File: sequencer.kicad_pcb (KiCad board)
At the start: 2 copper layers, 24 parts, among them SW1 B3S-1000P, SW2 B3S-1000P, SW3 B3S-1000P, SW4 B3S-1000P, SW5 B3S-1000P, SW6 B3S-1000P, SW7 B3S-1000P, SW8 B3S-1000P, SW9 B3S-1000P, U3 STM32F031K6Tx, U6 L78L05_SOT89, U7 L78L33_SOT89, Y1 8MHz

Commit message: mostly complete placement
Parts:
- removed the U6 at (78.5, 55.5)
- removed Y1: 8MHz, Crystal:Crystal_SMD_HC49-SD
- added C1: 100n, Capacitor_SMD:C_0603_1608Metric, B.Cu at (86.9, 93.0)
- added C10: 100n, Capacitor_SMD:C_0603_1608Metric, B.Cu at (103.0, 83.0)
- added C11: 100n, Capacitor_SMD:C_0603_1608Metric, B.Cu at (118.0, 83.0)
- added C13: 100n, Capacitor_SMD:C_0603_1608Metric, B.Cu at (147.0, 83.0)
- added C14: 100n, Capacitor_SMD:C_0603_1608Metric, B.Cu at (162.0, 83.0)
- added C15: 100n, Capacitor_SMD:C_0603_1608Metric, B.Cu at (177.0, 83.0)
- added C16: 100n, Capacitor_SMD:C_0603_1608Metric, B.Cu at (192.0, 83.0)
- added C17: 100n, Capacitor_SMD:C_0603_1608Metric, B.Cu at (154.0, 145.0)
- added C18: 100n, Capacitor_SMD:C_0603_1608Metric, B.Cu at (163.0, 143.0)
- added C19: 100n, Capacitor_SMD:C_0603_1608Metric, B.Cu at (202.0, 108.0)
- added C2: 100n, Capacitor_SMD:C_0603_1608Metric, B.Cu at (101.7, 93.0)
- added C20: 10n, Capacitor_SMD:C_0603_1608Metric, B.Cu at (149.0, 70.0)
- added C26: 100n, Capacitor_SMD:C_0603_1608Metric, B.Cu at (107.9, 119.0)
- added C27: 100n, Capacitor_SMD:C_0603_1608Metric, B.Cu at (122.8, 119.0)
- added C28: 330n, Capacitor_SMD:C_0805_2012Metric, B.Cu at (121.0, 39.0)
- added C29: 100n, Capacitor_SMD:C_0603_1608Metric, B.Cu at (121.0, 46.0)
- added C3: 100n, Capacitor_SMD:C_0603_1608Metric, B.Cu at (116.5, 93.0)
- added C30: 330n, Capacitor_SMD:C_0805_2012Metric, B.Cu at (117.0, 61.0)
- added C31: 100n, Capacitor_SMD:C_0603_1608Metric, B.Cu at (124.0, 61.0)
- added C4: 100n, Capacitor_SMD:C_0603_1608Metric, B.Cu at (131.3, 93.0)
- added C5: 100n, Capacitor_SMD:C_0603_1608Metric, B.Cu at (146.2, 93.0)
- added C8: 100n, Capacitor_SMD:C_0603_1608Metric, B.Cu at (190.6, 93.0)
- added C9: 100n, Capacitor_SMD:C_0603_1608Metric, B.Cu at (88.0, 83.0)
- added D3: Inolux_IN-PI554FCH, LED_SMD:LED_Inolux_IN-PI554FCH_PLCC4_5.0x5.0mm_P3.2mm, F.Cu at (117.8, 78.5)
- added D4: Inolux_IN-PI554FCH, LED_SMD:LED_Inolux_IN-PI554FCH_PLCC4_5.0x5.0mm_P3.2mm, F.Cu at (132.6, 78.5)
- added D5: Inolux_IN-PI554FCH, LED_SMD:LED_Inolux_IN-PI554FCH_PLCC4_5.0x5.0mm_P3.2mm, F.Cu at (147.4, 78.5)
- added D6: Inolux_IN-PI554FCH, LED_SMD:LED_Inolux_IN-PI554FCH_PLCC4_5.0x5.0mm_P3.2mm, F.Cu at (162.2, 78.5)
- added D7: Inolux_IN-PI554FCH, LED_SMD:LED_Inolux_IN-PI554FCH_PLCC4_5.0x5.0mm_P3.2mm, F.Cu at (177.0, 78.5)
- added D8: Inolux_IN-PI554FCH, LED_SMD:LED_Inolux_IN-PI554FCH_PLCC4_5.0x5.0mm_P3.2mm, F.Cu at (191.8, 78.5)
- added D9: red, LED_SMD:LED_0603_1608Metric, B.Cu at (99.0, 48.5)
- added G***: LOGO, Symbol_CreativeCommons:CC-BY-SA_SolderMaskTop_Small, B.Cu at (185.0, 68.0)
- added J1: AudioJack2_SwitchT, Connector_Audio:Jack_3.5mm_QingPu_WQP-PJ398SM_Vertical_CircularHoles, F.Cu at (96.0, 110.2)
- added J2: AudioJack2_SwitchT, Connector_Audio:Jack_3.5mm_QingPu_WQP-PJ398SM_Vertical_CircularHoles, F.Cu at (184.0, 110.2)
- added J3: AudioJack2_SwitchT, Connector_Audio:Jack_3.5mm_QingPu_WQP-PJ398SM_Vertical_CircularHoles, F.Cu at (172.9, 110.2)
- added J4: Conn_ARM_JTAG_SWD_10, Connector_PinHeader_1.27mm:PinHeader_2x05_P1.27mm_Vertical_SMD, B.Cu at (119.0, 70.0)
- added J5: Conn_01x06_Male, Connector_PinHeader_2.54mm:PinHeader_1x06_P2.54mm_Vertical, F.Cu at (139.3, 67.0)
- added J6: Conn_01x02_Male, Connector_Molex:Molex_SL_171971-0002_1x02_P2.54mm_Vertical, B.Cu at (93.0, 70.0)
- added R1: 10k, Resistor_SMD:R_0603_1608Metric, B.Cu at (104.0, 48.5)
- added R3: 1k, Resistor_SMD:R_0603_1608Metric, B.Cu at (101.0, 123.0)
- added REF**: MountingHole_3.2mm_M3, MountingHole:MountingHole_3.2mm_M3, F.Cu at (85.0, 70.0)
- added REF**: MountingHole_3.2mm_M3, MountingHole:MountingHole_3.2mm_M3, F.Cu at (195.0, 70.0)
- added REF**: MountingHole_3.2mm_M3, MountingHole:MountingHole_3.2mm_M3, F.Cu at (85.0, 120.0)
- added REF**: MountingHole_3.2mm_M3, MountingHole:MountingHole_3.2mm_M3, F.Cu at (195.0, 120.0)
- added RV1: 10k, Potentiometer_THT:Potentiometer_Bourns_PTV09A-1_Single_Vertical, F.Cu at (90.7, 96.0)
- added RV10: 10k, Potentiometer_THT:Potentiometer_Bourns_PTV09A-1_Single_Vertical, F.Cu at (126.5, 122.0)
- added RV2: 10k, Potentiometer_THT:Potentiometer_Bourns_PTV09A-1_Single_Vertical, F.Cu at (105.5, 96.0)
- added RV3: 10k, Potentiometer_THT:Potentiometer_Bourns_PTV09A-1_Single_Vertical, F.Cu at (120.3, 96.0)
- added RV4: 10k, Potentiometer_THT:Potentiometer_Bourns_PTV09A-1_Single_Vertical, F.Cu at (135.1, 96.0)
- added RV5: 10k, Potentiometer_THT:Potentiometer_Bourns_PTV09A-1_Single_Vertical, F.Cu at (149.9, 96.0)
- added RV6: 10k, Potentiometer_THT:Potentiometer_Bourns_PTV09A-1_Single_Vertical, F.Cu at (164.7, 96.0)
- added RV7: 10k, Potentiometer_THT:Potentiometer_Bourns_PTV09A-1_Single_Vertical, F.Cu at (179.5, 96.0)
- added RV8: 10k, Potentiometer_THT:Potentiometer_Bourns_PTV09A-1_Single_Vertical, F.Cu at (194.3, 96.0)
- added RV9: 10k, Potentiometer_THT:Potentiometer_Bourns_PTV09A-1_Single_Vertical, F.Cu at (111.7, 122.0)
- added SW10: SW_SPST, Button_Switch_THT_gkeeth:SW_Toggle_SPST_NKK_M2011xxx03, F.Cu at (92.0, 58.0)
- added U1: LM358, Package_SO:SOIC-8_3.9x4.9mm_P1.27mm, B.Cu at (194.0, 110.0)
- added U2: 74HC4051, Package_SO:SOIC-16_3.9x9.9mm_P1.27mm, B.Cu at (154.0, 136.0)
- added U4: 74HCT14, Package_SO:SOIC-14_3.9x8.7mm_P1.27mm, B.Cu at (163.0, 136.0)
- added U5: L78L05_SOT89, Package_TO_SOT_SMD:SOT-89-3, B.Cu at (121.7, 42.5)
- added X1: ASV-8.000MHz, Oscillator:Oscillator_SMD_Abracon_ASV-4Pin_7.0x5.1mm, B.Cu at (144.0, 71.0)
- C12, U3: moved to B.Cu
- C21: renamed from C5; moved to B.Cu
- C22: renamed from C8; moved to B.Cu
- C23: renamed from C9; moved to B.Cu
- C24: renamed from C10; moved to B.Cu
- C25: renamed from C11; moved to B.Cu
- C6, C7: value 27p -> 100n; moved to B.Cu
- R2: renamed from R10; moved to B.Cu
- SW1, SW2, SW3, SW4, SW5, SW6, SW7, SW8, SW9: value B3S-1000P -> OS102011MS2QN1; footprint Button_Switch_SMD:SW_SPST_B3S-1000 -> Button_Switch_THT:SW_Slide_1P2T_CK_OS102011MS2Q
- U6: renamed from U7; moved to B.Cu
- moved SW8 125.4 mm to (189.8, 101.0)
- moved SW7 117.5 mm to (175.0, 101.0)
- moved C7 106.1 mm to (175.8, 93.0)
- moved SW6 105.0 mm to (160.2, 101.0)
- moved SW5 97.6 mm to (145.4, 101.0)
- moved C6 95.9 mm to (161.0, 93.0)
- moved SW4 92.7 mm to (130.6, 101.0)
- moved SW9 91.0 mm to (136.0, 120.3)
- moved C22 87.6 mm to (141.0, 77.0), turned to -90 degrees
- moved SW3 78.0 mm to (115.8, 101.0)
- moved SW1 75.0 mm to (86.2, 101.0)
- moved SW2 74.6 mm to (101.0, 101.0)
- moved C25 71.9 mm to (125.0, 80.0), turned to -90 degrees
- moved C21 70.5 mm to (139.0, 77.0), turned to -90 degrees
- moved C12 61.6 mm to (133.0, 83.0)
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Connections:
- net /skip_button_1 renamed /skip_switch_1
- net /skip_button_2 renamed /skip_switch_2
- net /skip_button_3 renamed /skip_switch_3
- net /skip_button_4 renamed /skip_switch_4
- net /skip_button_5 renamed /skip_switch_5
- net /skip_button_6 renamed /skip_switch_6
- net /skip_button_7 renamed /skip_switch_7
- net /skip_button_8 renamed /skip_switch_8
- C12 pad 1: GND -> +5V
- C12 pad 2: Net-(J4-~{RESET}) -> GND
- C6 pad 1: Net-(U3-PF0) -> GND
- C6 pad 2: GND -> /cv_pot_6
- C7 pad 1: Net-(U3-PF1) -> GND
- C7 pad 2: GND -> /cv_pot_7
- D1 pad 2: unconnected-(D1-DIN) -> /led_ctrl
- D1 pad 4: unconnected-(D1-DO) -> Net-(D1-DO)
- D2 pad 2: unconnected-(D2-DIN) -> Net-(D1-DO)
- D2 pad 4: unconnected-(D2-DO) -> Net-(D2-DO)
- SW1 pad 1: GND -> +5V
- SW2 pad 1: GND -> +5V
- SW3 pad 1: GND -> +5V
- SW4 pad 1: GND -> +5V
- SW5 pad 1: GND -> +5V
- SW6 pad 1: GND -> +5V
- SW7 pad 1: GND -> +5V
- SW8 pad 1: GND -> +5V
- SW9 pad 1: GND -> +5V
- SW9 pad 2: Net-(J4-~{RESET}) -> /skip_reset_switch
- U3 pad 14: unconnected-(U3-PB0) -> /duty_pot
- U3 pad 18: unconnected-(U3-PA8) -> /skip_reset_switch
- U3 pad 2: Net-(U3-PF0) -> /clkin
- U3 pad 21: unconnected-(U3-PA11) -> /internal_clock
- U3 pad 25: unconnected-(U3-PA15) -> Net-(D9-A)
- U3 pad 26: /internal_clock -> /led_ctrl
- U3 pad 3: Net-(U3-PF1) -> unconnected-(U3-PF1)
- U3 pad 4: Net-(J4-~{RESET}) -> /NRST
- U6 pad 1: unconnected-(U7-OUT) -> +3.3V
- U6 pad 2: unconnected-(U7-GND) -> GND
- U6 pad 3: unconnected-(U7-IN) -> +9V
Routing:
- added copper zone on In1.Cu, net GND
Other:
- board outline added: 120 x 60 mm
- copper layers 2 -> 4

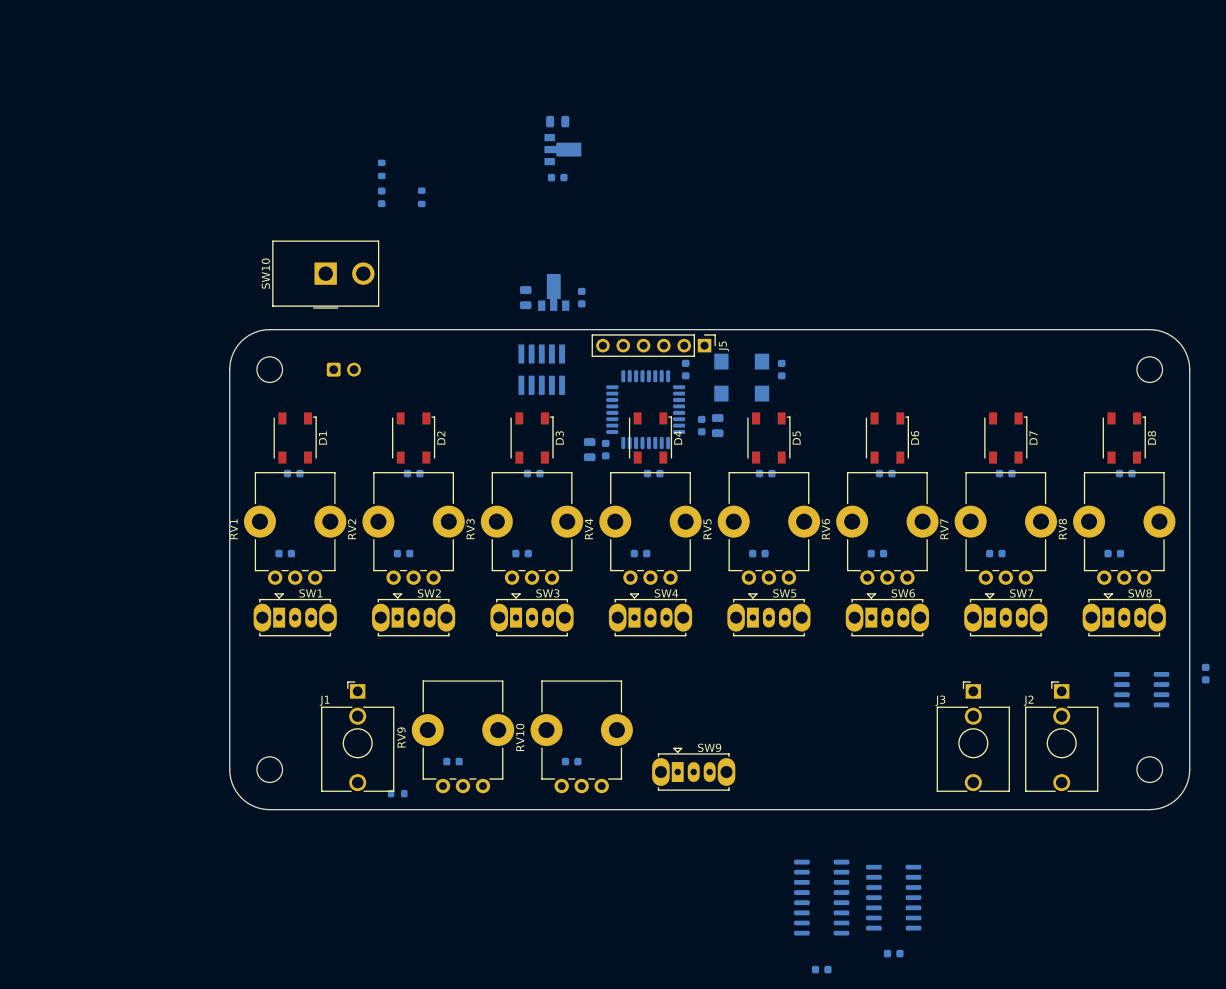
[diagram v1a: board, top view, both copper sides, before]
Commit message: initial routing complete, DRC errors clean
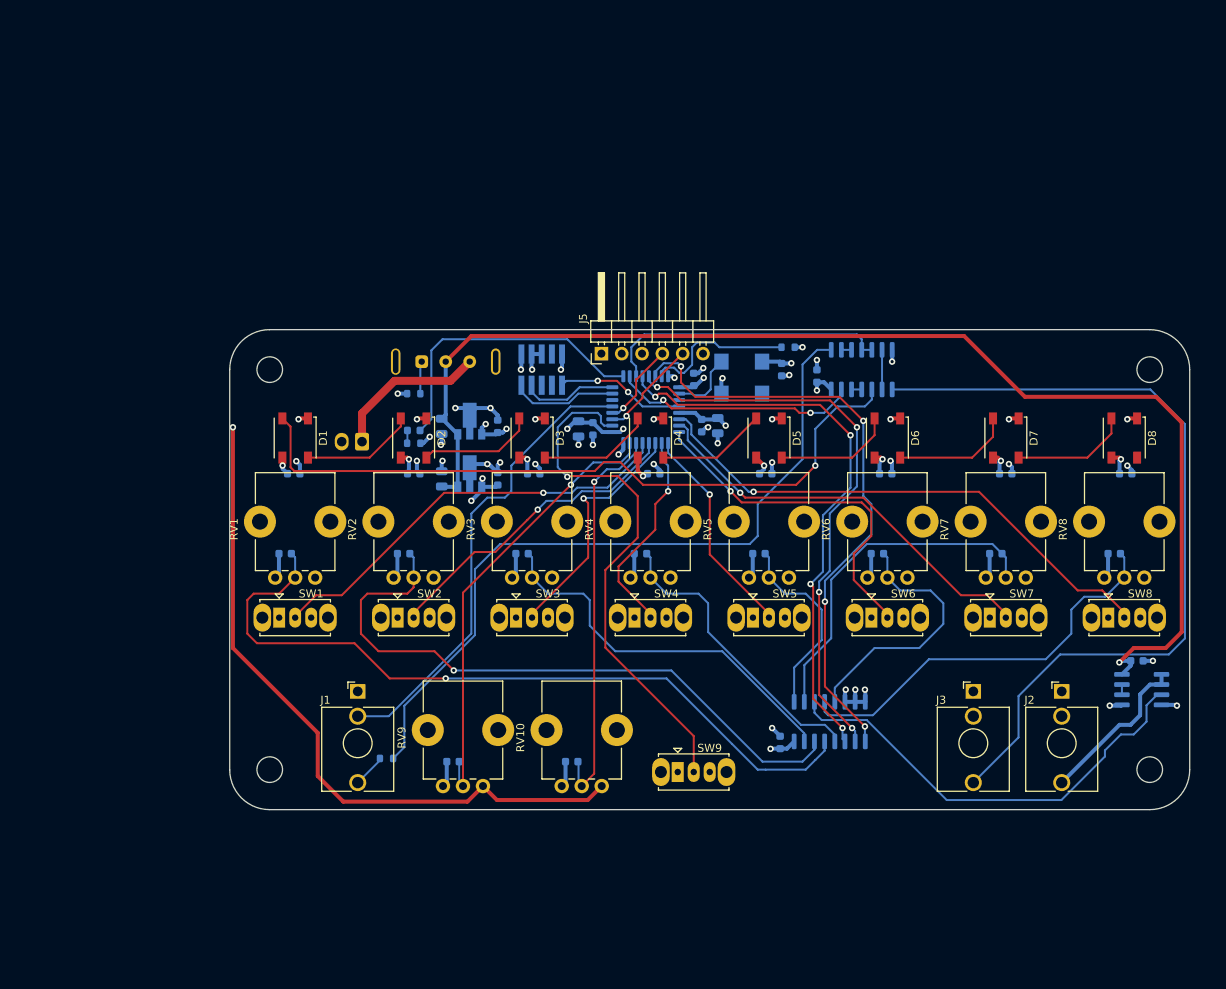
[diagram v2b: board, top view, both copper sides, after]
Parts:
- added R4: 10k, Resistor_SMD:R_0603_1608Metric, B.Cu at (103.0, 73.0)
- J5: footprint Connector_PinHeader_2.54mm:PinHeader_1x06_P2.54mm_Vertical -> Connector_PinHeader_2.54mm:PinHeader_1x06_P2.54mm_Horizontal
- J6: footprint Connector_Molex:Molex_SL_171971-0002_1x02_P2.54mm_Vertical -> Connector_Molex_SL:Molex_SL_A-70553-0001_1x02_P2.54mm_Horizontal
- SW10: value SW_SPST -> EG1206A; footprint Button_Switch_THT_gkeeth:SW_Toggle_SPST_NKK_M2011xxx03 -> Button_Switch_THT_gkeeth:SW_Slide_SPDT_E-Switch_EG1206A; moved to B.Cu
- moved C18 72.8 mm to (153.4, 70.8), turned to -90 degrees
- moved U4 66.1 mm to (159.0, 70.0), turned to -90 degrees
- moved R1 49.5 mm to (149.8, 67.2), turned to 180 degrees
- moved C28 46.9 mm to (106.5, 83.7), turned to 90 degrees
- moved U5 42.1 mm to (110.0, 83.0), turned to 90 degrees
- moved C29 38.4 mm to (113.5, 83.7), turned to -90 degrees
- moved R2 34.5 mm to (103.0, 79.2), turned to 180 degrees
- moved D9 29.4 mm to (103.0, 77.6), turned to 0 degrees
- moved C17 28.9 mm to (148.8, 116.6), turned to -90 degrees
- moved U2 22.0 mm to (155.0, 114.0), turned to -90 degrees
- moved C30 19.2 mm to (106.5, 77.1)
- moved C31 19.2 mm to (113.5, 77.1)
- moved U6 19.2 mm to (110.0, 76.4)
- moved SW10 16.3 mm to (104.0, 69.0), turned to 0 degrees
- moved J5 12.9 mm to (126.5, 68.0), turned to 90 degrees
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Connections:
- net Net-(D9-A) renamed /RED_LED
- D1 pad 2: /led_ctrl -> /led_ctrl_5v
- J1 pad T: /selected_clock_unbuffered -> Net-(J1-PadT)
- R3 pad 1: /selected_clock_unbuffered -> Net-(J1-PadT)
- R3 pad 2: Net-(R3-Pad2) -> /selected_clock_unbuffered
- SW10 pad 1: Net-(J6-Pin_1) -> Net-(SW10-A)
- U3 pad 10: /skip_switch_5 -> /skip_switch_4
- U3 pad 11: /skip_switch_6 -> /skip_switch_3
- U3 pad 12: /skip_switch_7 -> /skip_switch_2
- U3 pad 13: /skip_switch_8 -> /skip_switch_1
- U3 pad 26: /led_ctrl -> /led_ctrl_3v3
- U3 pad 6: /skip_switch_1 -> /skip_switch_8
- U3 pad 7: /skip_switch_2 -> /skip_switch_7
- U3 pad 8: /skip_switch_3 -> /skip_switch_6
- U3 pad 9: /skip_switch_4 -> /skip_switch_5
- U4 pad 1: Net-(R3-Pad2) -> /selected_clock_unbuffered
- U4 pad 10: unconnected-(U4-Pad10) -> /led_ctrl_5v
- U4 pad 11: GND -> /~{led_ctrl_5v}
- U4 pad 12: unconnected-(U4-Pad12) -> /~{led_ctrl_5v}
- U4 pad 13: GND -> /led_ctrl_3v3
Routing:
- net +9V: track 0.00 -> 155.8 mm, vias 0 -> 1
- net +3.3V: track 0.00 -> 116.0 mm, vias 0 -> 9
- net GND: track 0.00 -> 113.4 mm, vias 0 -> 45
- net /clock_out_buffered: track 0.00 -> 102.1 mm
- net /cv_pot_1: track 0.00 -> 95.9 mm, vias 0 -> 1
- net /selected_clock_unbuffered: track 0.00 -> 93.1 mm
- net /led_ctrl_5v: track 0.00 -> 89.4 mm, vias 0 -> 1
- net /cv_pot_2: track 0.00 -> 80.8 mm, vias 0 -> 1
- net /step_sel2: track 0.00 -> 76.2 mm, vias 0 -> 4
- net /step_sel0: track 0.00 -> 72.1 mm, vias 0 -> 4
- net /step_sel1: track 0.00 -> 72.1 mm, vias 0 -> 4
- net /skip_switch_8: track 0.00 -> 67.0 mm, vias 0 -> 1
- net /skip_reset_switch: track 0.00 -> 66.0 mm, vias 0 -> 1
- net /internal_clock: track 0.00 -> 58.5 mm
- net /tempo_pot: track 0.00 -> 56.8 mm, vias 0 -> 1
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- added copper zone on In2.Cu, net +3.3V
- added copper zone on In2.Cu, net +5V

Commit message: DRC clean, moved refdeses
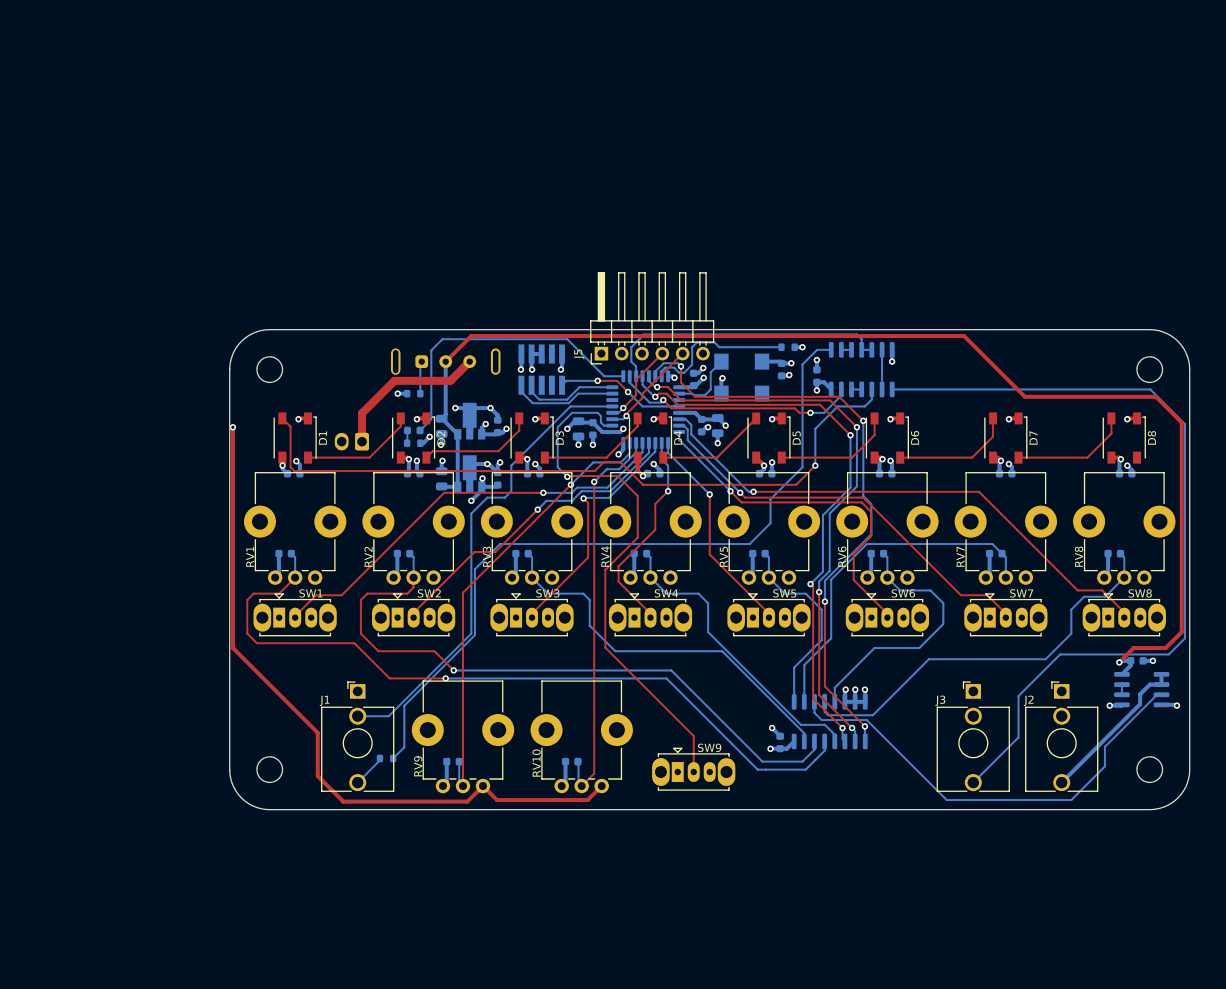
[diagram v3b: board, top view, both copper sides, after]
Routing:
- net /cv_out_buffered: track 20.3 -> 19.5 mm

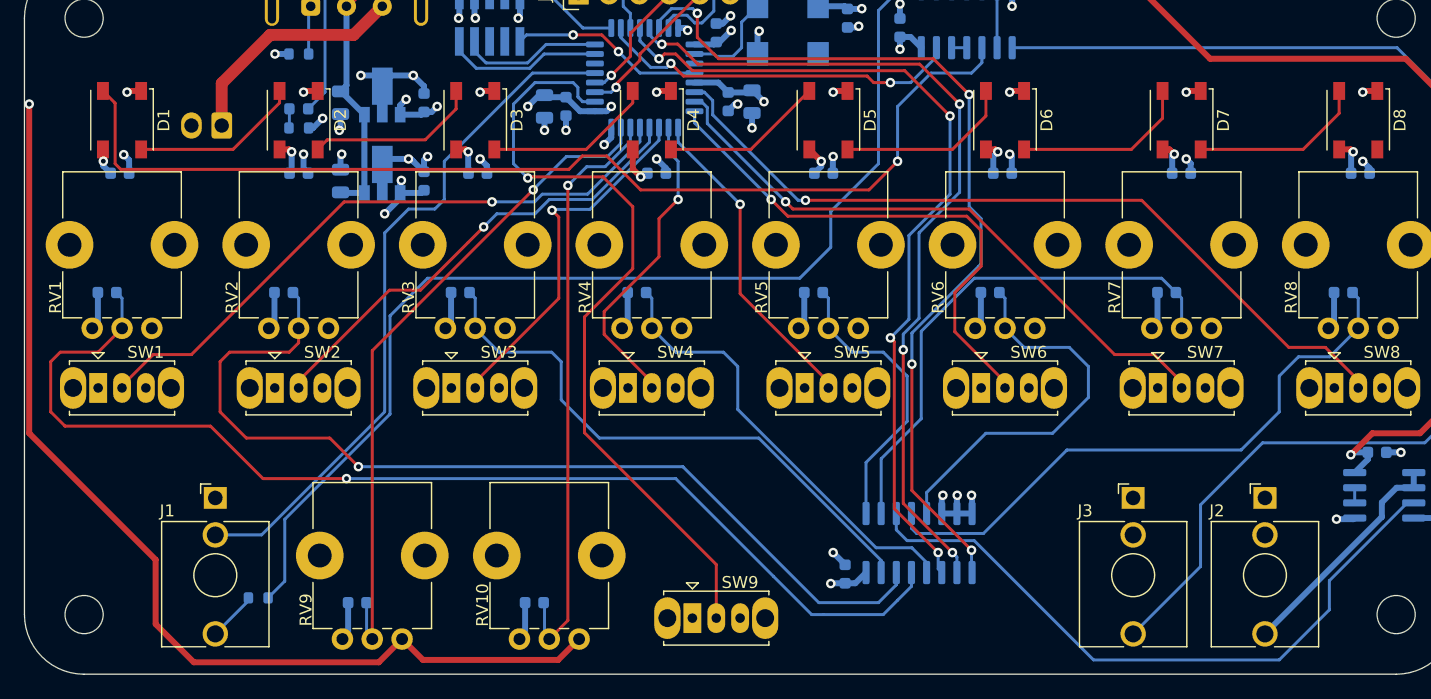
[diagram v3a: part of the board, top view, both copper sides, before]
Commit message: Circuit fixes and cleanup
- minor schematic rearranging
- checking I/O levels between MCU and 5V logic (still need to check
  switch selection bits)
- change switches to 3V3, re-route
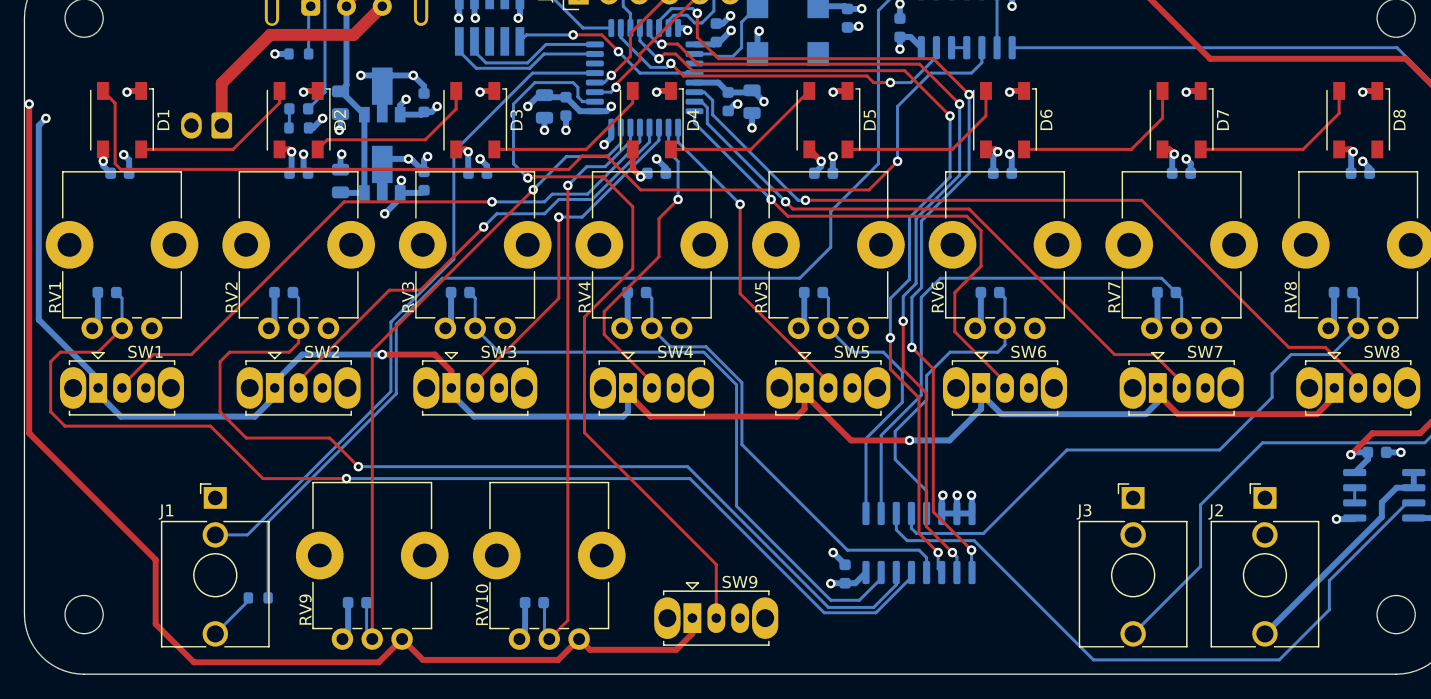
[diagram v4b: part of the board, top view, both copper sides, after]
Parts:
- removed G***: LOGO, Symbol_CreativeCommons:CC-BY-SA_SolderMaskTop_Small
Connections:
- SW1 pad 1: +5V -> +3.3V
- SW2 pad 1: +5V -> +3.3V
- SW3 pad 1: +5V -> +3.3V
- SW4 pad 1: +5V -> +3.3V
- SW5 pad 1: +5V -> +3.3V
- SW6 pad 1: +5V -> +3.3V
- SW7 pad 1: +5V -> +3.3V
- SW8 pad 1: +5V -> +3.3V
- SW9 pad 1: +5V -> +3.3V
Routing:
- net +3.3V: track 116.0 -> 279.5 mm, vias 9 -> 12
- net /cv_pot_6: track 32.7 -> 26.0 mm
- net /cv_pot_3: track 48.2 -> 53.9 mm
- net /internal_clock: track 58.5 -> 56.5 mm
- net /cv_pot_7: track 43.6 -> 45.2 mm
- net /cv_pot_4: track 37.3 -> 38.5 mm
- net /skip_switch_3: track 30.5 -> 29.4 mm
- net /step_sel2: track 76.2 -> 75.3 mm
- net /selected_clock_unbuffered: track 93.1 -> 92.3 mm
- net /cv_pot_8: track 51.0 -> 50.4 mm
- net /cv_pot_1: track 95.9 -> 95.3 mm
